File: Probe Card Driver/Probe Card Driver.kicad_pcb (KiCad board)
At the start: 4 copper layers, 84.8 x 169 mm, 38 parts, among them J1 BNC, J10 FCR7350R, J11 FCR7350R, J12 LDO_SAMPLE, J13 MEMS_PINOUT, J14 Conn_01x03_Pin, J15 Conn_01x02_Pin, J2 Conn_01x03_Pin, J3 FCR7350R, J4 FCR7350R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

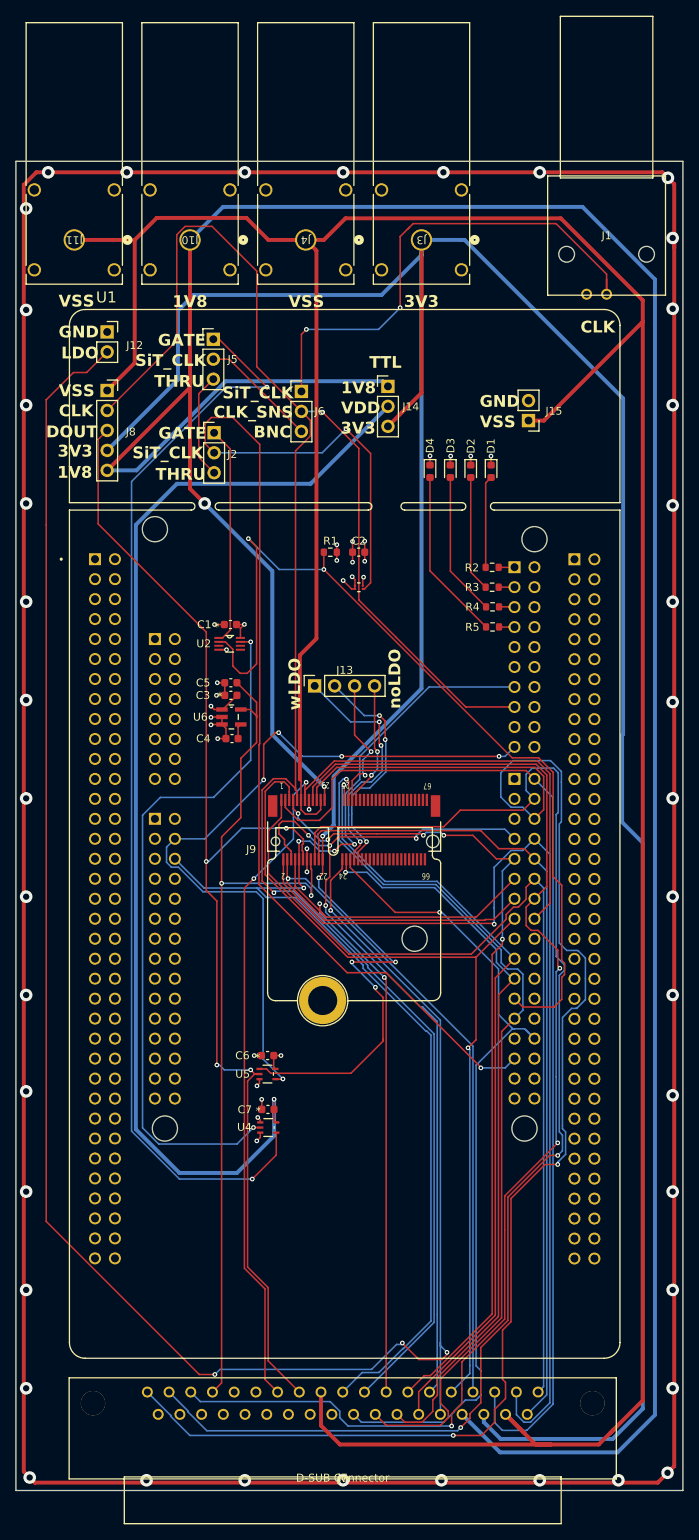
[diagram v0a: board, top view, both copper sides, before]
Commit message: Added BOM and Minor Updates
Added a BOM and included minor updates to layout and schematic.
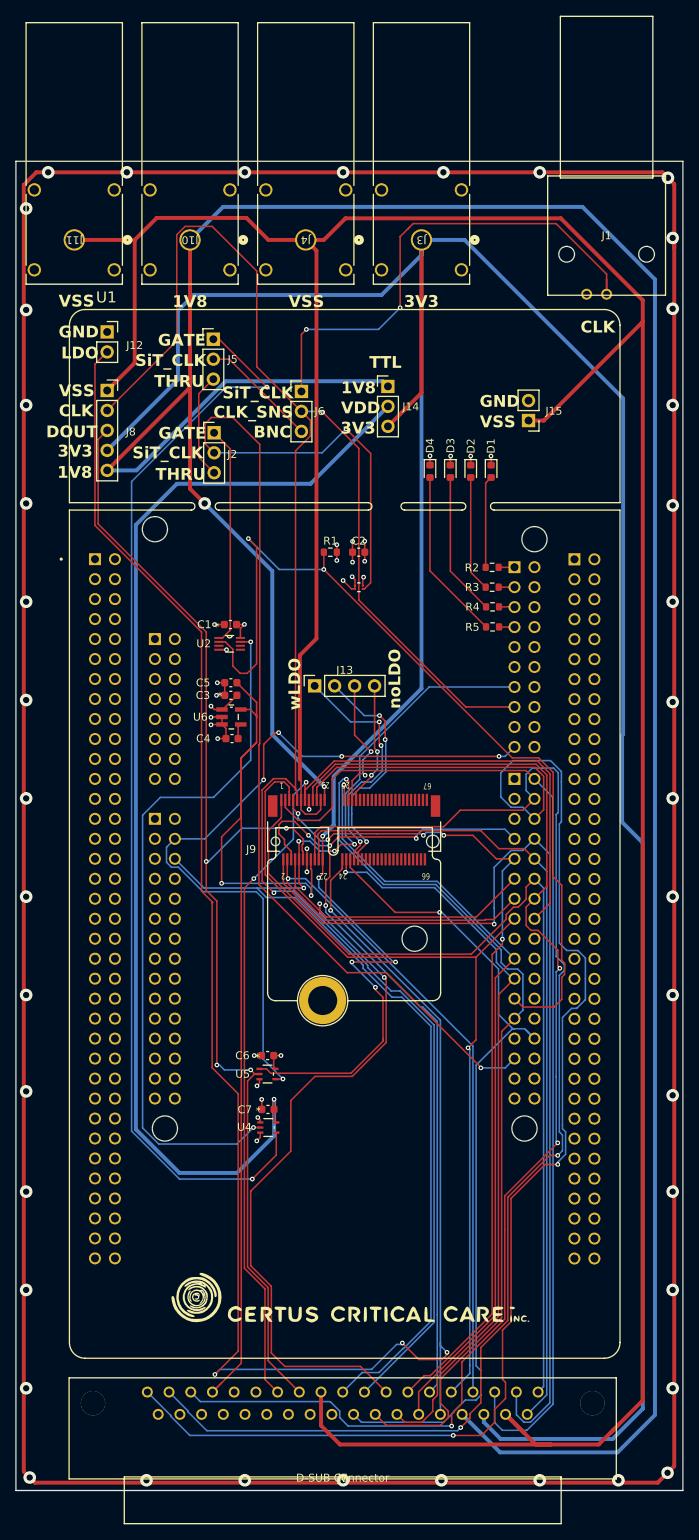
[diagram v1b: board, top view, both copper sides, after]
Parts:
- added G***: LOGO, InHouseFootprints:CertusHorizontalLogoFull, F.Cu at (172.4, 211.1)
- added G***: LOGO, InHouseFootprints:CertusHorizontalLogoFull, B.Cu at (172.0, 198.4)
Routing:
- net test_enable: track 102.3 -> 125.0 mm
- net +1V8: track 113.3 -> 134.7 mm
- net LDO_out: track 255.6 -> 250.9 mm
- net CLK_TO_SENSOR: track 260.5 -> 261.1 mm
- net D_OUT_TX_PD5_D53: track 149.3 -> 150.0 mm
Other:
- board text added: "TSMC Probe Card Driver August 28, 2024"
